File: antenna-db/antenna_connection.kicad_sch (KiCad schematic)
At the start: 2 parts

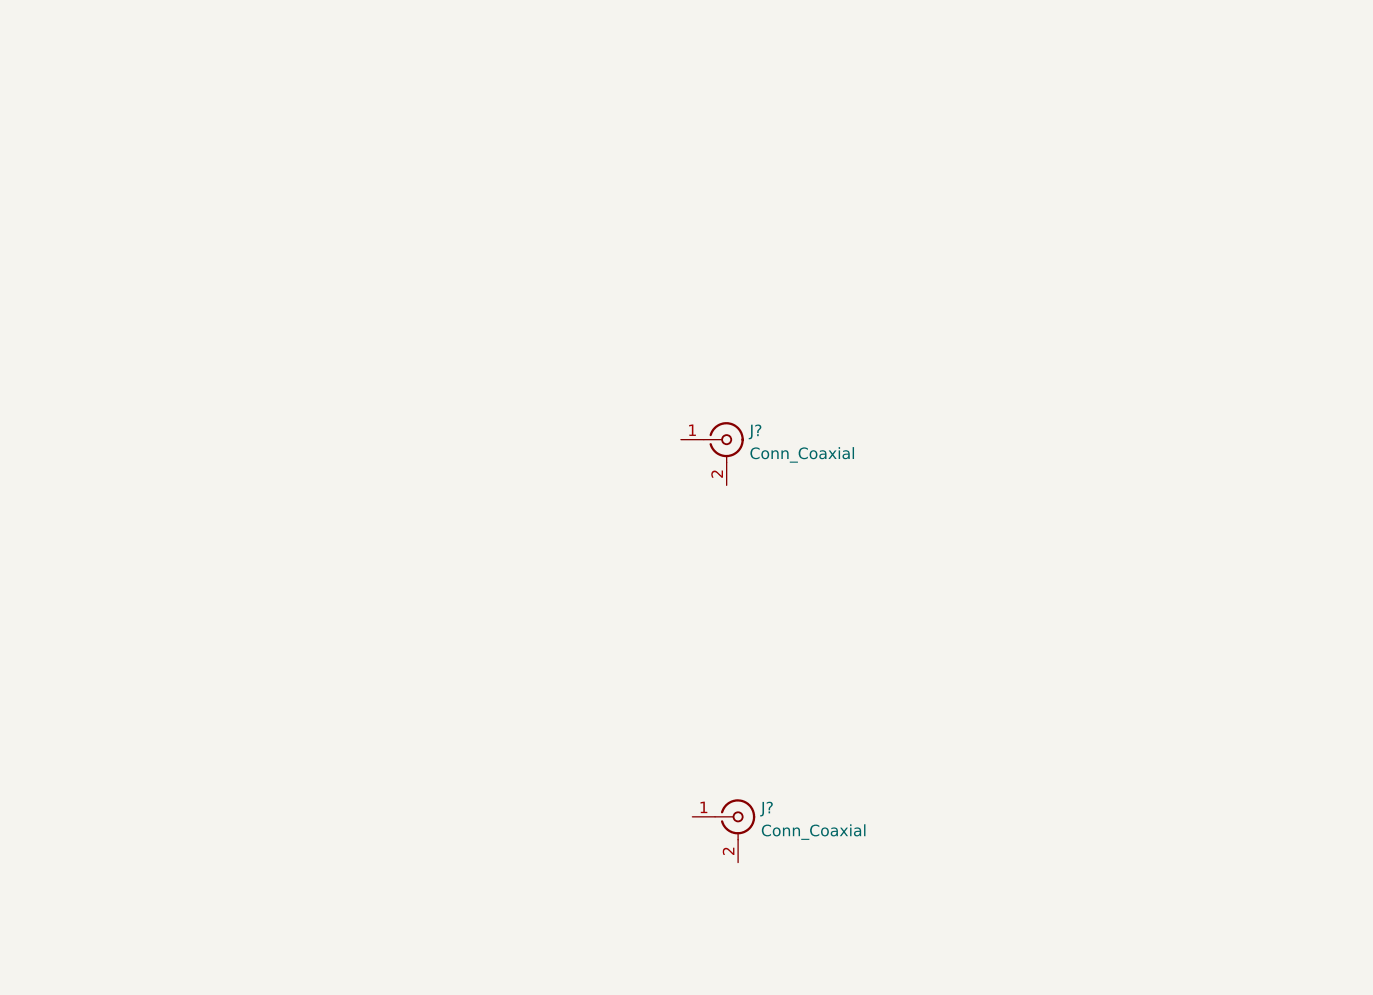
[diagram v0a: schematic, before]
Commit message: added baluns to antenna connection part
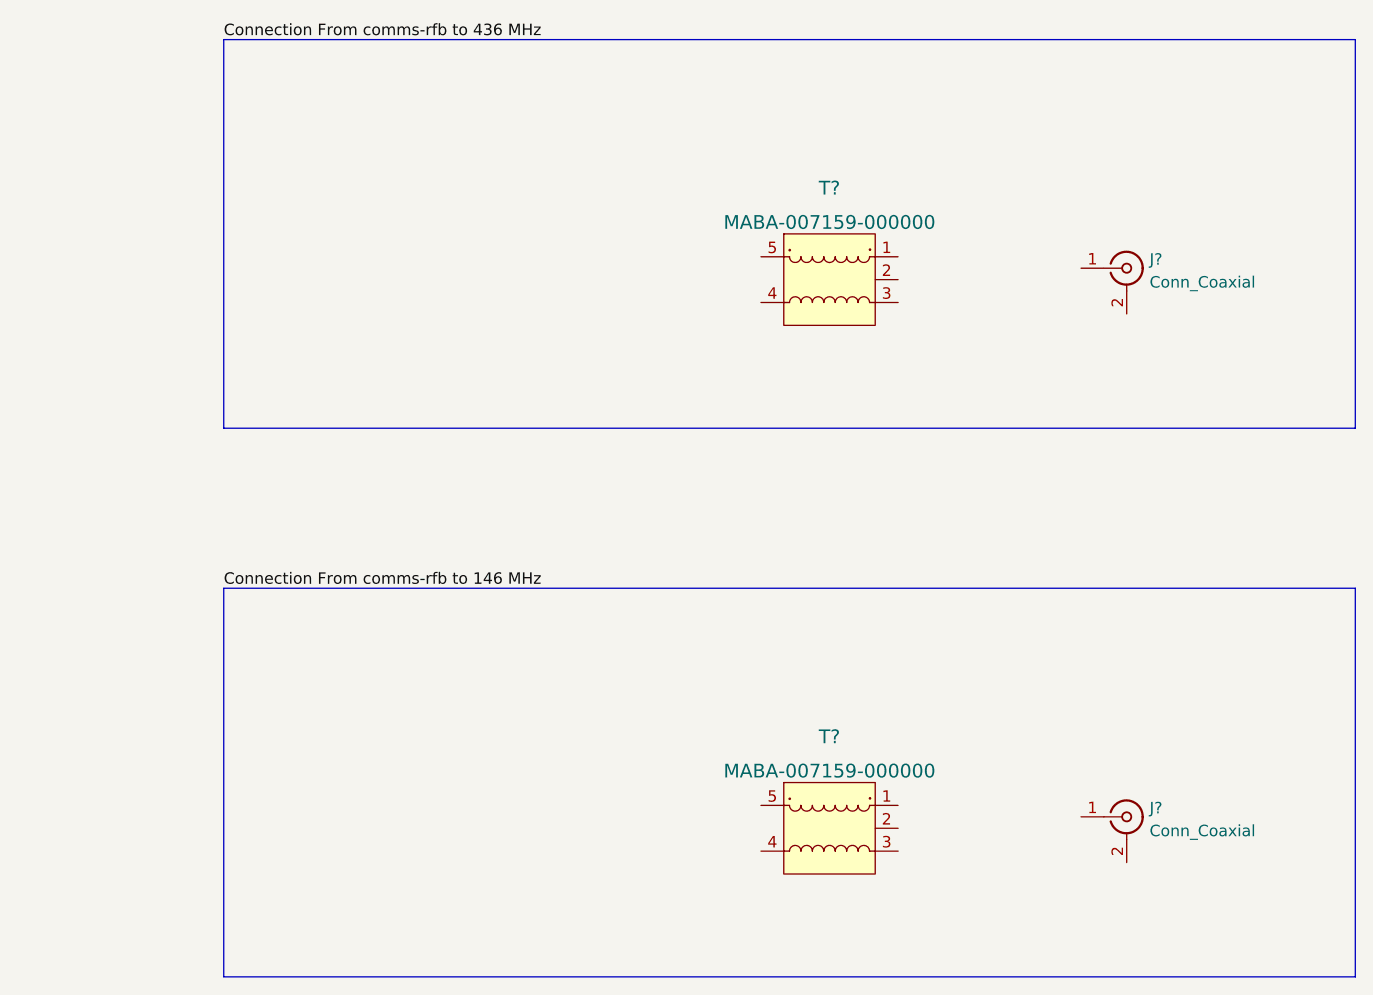
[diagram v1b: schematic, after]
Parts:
- removed J?: Conn_Coaxial, symbol Connector:Conn_Coaxial
- added J?: Conn_Coaxial, symbol Connector:Conn_Coaxial
- added T? (x2): MABA-007159-000000, digikey-footprints:SMD-5-6_3.83x2.79mm, symbol dk_Balun:MABA-007159-000000
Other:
- moved on the sheet: J?
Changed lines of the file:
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@@
 (kicad_sch (version 20211123) (generator eeschema)
   (paper "A4")
-  (symbol (lib_id "Connector:Conn_Coaxial") (at 160.02 80.01 0) (unit 1)
+  (polyline (pts (xy 104.14 96.52) (xy 229.87 96.52))
+    (stroke (width 0) (type default) (color 0 0 0 0))
+  )
+  (polyline (pts (xy 104.14 35.56) (xy 229.87 35.56))
+    (stroke (width 0) (type default) (color 0 0 0 0))
+  )
+  (polyline (pts (xy 229.87 78.74) (xy 104.14 78.74))
+    (stroke (width 0) (type default) (color 0 0 0 0))
+  )
+  (polyline (pts (xy 104.14 35.56) (xy 104.14 78.74))
+    (stroke (width 0) (type default) (color 0 0 0 0))
+  )
+  (polyline (pts (xy 104.14 96.52) (xy 104.14 139.7))
+    (stroke (width 0) (type default) (color 0 0 0 0))
+  )
+  (polyline (pts (xy 229.87 139.7) (xy 104.14 139.7))
+    (stroke (width 0) (type default) (color 0 0 0 0))
+  )
+  (polyline (pts (xy 229.87 96.52) (xy 229.87 139.7))
+    (stroke (width 0) (type default) (color 0 0 0 0))
+  )
+  (polyline (pts (xy 229.87 35.56) (xy 229.87 78.74))
+    (stroke (width 0) (type default) (color 0 0 0 0))
+  )
+  (label "Connection From comms-rfb to 146 MHz" (at 104.14 96.52 0)
+    (effects (font (size 1.27 1.27)) (justify left bottom))
+  )
+  (label "Connection From comms-rfb to 436 MHz" (at 104.14 35.56 0)
+    (effects (font (size 1.27 1.27)) (justify left bottom))
+  )
+  (symbol (lib_id "Connector:Conn_Coaxial") (at 204.47 60.96 0) (unit 1)
     (in_bom yes) (on_board yes) (fields_autoplaced)
-    (property "Reference" "J?" (id 0) (at 162.56 79.0331 0)
+    (property "Reference" "J?" (id 0) (at 207.01 59.9831 0)
       (effects (font (size 1.27 1.27)) (justify left))
     )
-    (property "Value" "Conn_Coaxial" (id 1) (at 162.56 81.5731 0)
+    (property "Value" "Conn_Coaxial" (id 1) (at 207.01 62.5231 0)
       (effects (font (size 1.27 1.27)) (justify left))
     )
-    (property "Footprint" "" (id 2) (at 160.02 80.01 0)
+    (property "Footprint" "" (id 2) (at 204.47 60.96 0)
       (effects (font (size 1.27 1.27)) hide)
     )
-    (property "Datasheet" " ~" (id 3) (at 160.02 80.01 0)
+    (property "Datasheet" " ~" (id 3) (at 204.47 60.96 0)
       (effects (font (size 1.27 1.27)) hide)
     )
@@
     (pin "2")
   )
-  (symbol (lib_id "Connector:Conn_Coaxial") (at 161.29 121.92 0) (unit 1)
+  (symbol (lib_id "dk_Balun:MABA-007159-000000") (at 171.45 62.23 0) (unit 1)
     (in_bom yes) (on_board yes) (fields_autoplaced)
-    (property "Reference" "J?" (id 0) (at 163.83 120.9431 0)
+    (property "Reference" "T?" (id 0) (at 171.45 52.07 0)
+      (effects (font (size 1.524 1.524)))
+    )
+    (property "Value" "MABA-007159-000000" (id 1) (at 171.45 55.88 0)
+      (effects (font (size 1.524 1.524)))
+    )
+    (property "Footprint" "digikey-footprints:SMD-5-6_3.83x2.79mm" (id 2) (at 176.53 57.15 0)
+      (effects (font (size 1.524 1.524)) (justify left) hide)
+    )
+    (property "Datasheet" "http://cdn.macom.com/datasheets/MABA-007159-000000.pdf" (id 3) (at 176.53 54.61 0)
+      (effects (font (size 1.524 1.524)) (justify left) hide)
+    )
+    (property "Digi-Key_PN" "1465-1302-1-ND" (id 4) (at 176.53 52.07 0)
+      (effects (font (size 1.524 1.524)) (justify left) hide)
+    )
+    (property "MPN" "MABA-007159-000000" (id 5) (at 176.53 49.53 0)
+      (effects (font (size 1.524 1.524)) (justify left) hide)
+    )
+    (property "Category" "RF/IF and RFID" (id 6) (at 176.53 46.99 0)
+      (effects (font (size 1.524 1.524)) (justify left) hide)
+    )
+    (property "Family" "Balun" (id 7) (at 176.53 44.45 0)
+      (effects (font (size 1.524 1.524)) (justify left) hide)
+    )
+    (property "DK_Datasheet_Link" "http://cdn.macom.com/datasheets/MABA-007159-000000.pdf" (id 8) (at 176.53 41.91 0)
+      (effects (font (size 1.524 1.524)) (justify left) hide)
+    )
+    (property "DK_Detail_Page" "/product-detail/en/m-a-com-technology-solutions/MABA-007159-000000/1465-1302-1-ND/4429999" (id 9) (at 176.53 39.37 0)
+      (effects (font (size 1.524 1.524)) (justify left) hide)
+    )
+    (property "Description" "BALUN 4.5MHZ-3GHZ 1:1 6SMD FLAT" (id 10) (at 176.53 36.83 0)
+      (effects (font (size 1.524 1.524)) (justify left) hide)
+    )
+    (property "Manufacturer" "M/A-Com Technology Solutions" (id 11) (at 176.53 34.29 0)
+      (effects (font (size 1.524 1.524)) (justify left) hide)
+    )
+    (property "Status" "Active" (id 12) (at 176.53 31.75 0)
+      (effects (font (size 1.524 1.524)) (justify left) hide)
+    )
+    (pin "2")
+    (pin "1")
+    (pin "3")
+    (pin "4")
+    (pin "5")
+  )
+  (symbol (lib_id "dk_Balun:MABA-007159-000000") (at 171.45 123.19 0) (unit 1)
+    (in_bom yes) (on_board yes) (fields_autoplaced)
+    (property "Reference" "T?" (id 0) (at 171.45 113.03 0)
+      (effects (font (size 1.524 1.524)))
+    )
+    (property "Value" "MABA-007159-000000" (id 1) (at 171.45 116.84 0)
+      (effects (font (size 1.524 1.524)))
+    )
+    (property "Footprint" "digikey-footprints:SMD-5-6_3.83x2.79mm" (id 2) (at 176.53 118.11 0)
+      (effects (font (size 1.524 1.524)) (justify left) hide)
+    )
+    (property "Datasheet" "http://cdn.macom.com/datasheets/MABA-007159-000000.pdf" (id 3) (at 176.53 115.57 0)
+      (effects (font (size 1.524 1.524)) (justify left) hide)
+    )
+    (property "Digi-Key_PN" "1465-1302-1-ND" (id 4) (at 176.53 113.03 0)
+      (effects (font (size 1.524 1.524)) (justify left) hide)
+    )
+    (property "MPN" "MABA-007159-000000" (id 5) (at 176.53 110.49 0)
+      (effects (font (size 1.524 1.524)) (justify left) hide)
+    )
+    (property "Category" "RF/IF and RFID" (id 6) (at 176.53 107.95 0)
+      (effects (font (size 1.524 1.524)) (justify left) hide)
+    )
+    (property "Family" "Balun" (id 7) (at 176.53 105.41 0)
+      (effects (font (size 1.524 1.524)) (justify left) hide)
+    )
+    (property "DK_Datasheet_Link" "http://cdn.macom.com/datasheets/MABA-007159-000000.pdf" (id 8) (at 176.53 102.87 0)
+      (effects (font (size 1.524 1.524)) (justify left) hide)
+    )
+    (property "DK_Detail_Page" "/product-detail/en/m-a-com-technology-solutions/MABA-007159-000000/1465-1302-1-ND/4429999" (id 9) (at 176.53 100.33 0)
+      (effects (font (size 1.524 1.524)) (justify left) hide)
+    )
+    (property "Description" "BALUN 4.5MHZ-3GHZ 1:1 6SMD FLAT" (id 10) (at 176.53 97.79 0)
+      (effects (font (size 1.524 1.524)) (justify left) hide)
+    )
+    (property "Manufacturer" "M/A-Com Technology Solutions" (id 11) (at 176.53 95.25 0)
+      (effects (font (size 1.524 1.524)) (justify left) hide)
+    )
+    (property "Status" "Active" (id 12) (at 176.53 92.71 0)
+      (effects (font (size 1.524 1.524)) (justify left) hide)
+    )
+    (pin "2")
+    (pin "1")
+    (pin "3")
+    (pin "4")
+    (pin "5")
+  )
+  (symbol (lib_id "Connector:Conn_Coaxial") (at 204.47 121.92 0) (unit 1)
+    (in_bom yes) (on_board yes) (fields_autoplaced)
+    (property "Reference" "J?" (id 0) (at 207.01 120.9431 0)
       (effects (font (size 1.27 1.27)) (justify left))
     )
-    (property "Value" "Conn_Coaxial" (id 1) (at 163.83 123.4831 0)
+    (property "Value" "Conn_Coaxial" (id 1) (at 207.01 123.4831 0)
       (effects (font (size 1.27 1.27)) (justify left))
     )
-    (property "Footprint" "" (id 2) (at 161.29 121.92 0)
+    (property "Footprint" "" (id 2) (at 204.47 121.92 0)
       (effects (font (size 1.27 1.27)) hide)
     )
-    (property "Datasheet" " ~" (id 3) (at 161.29 121.92 0)
+    (property "Datasheet" " ~" (id 3) (at 204.47 121.92 0)
       (effects (font (size 1.27 1.27)) hide)
     )

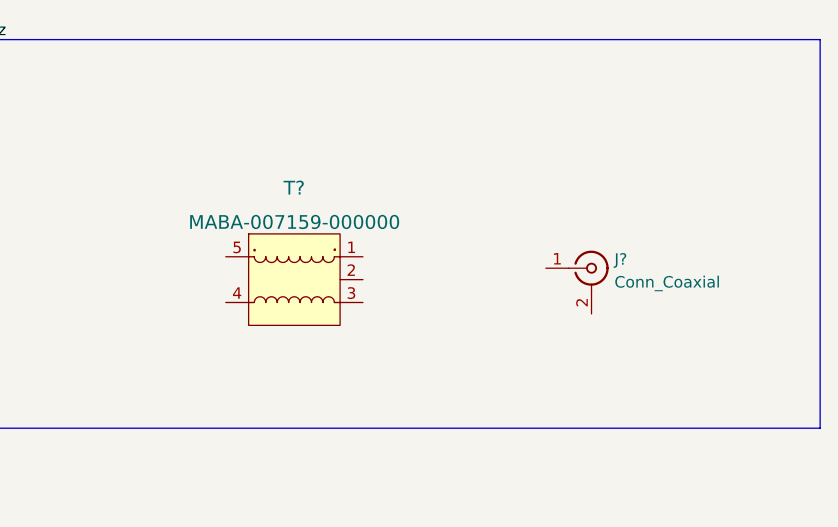
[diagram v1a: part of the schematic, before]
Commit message: added regulator symbol ~ not circuit yet
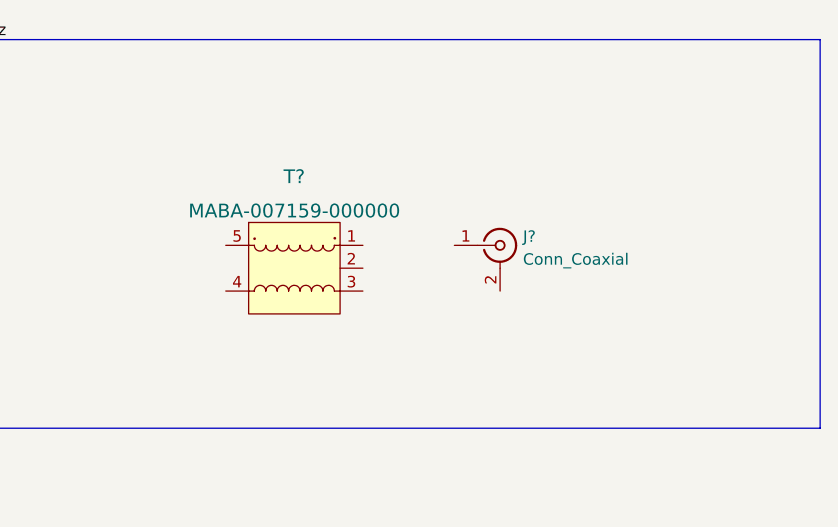
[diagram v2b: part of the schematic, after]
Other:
- moved on the sheet: J?, T?
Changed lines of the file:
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@@
     (effects (font (size 1.27 1.27)) (justify left bottom))
   )
-  (symbol (lib_id "Connector:Conn_Coaxial") (at 204.47 60.96 0) (unit 1)
+  (symbol (lib_id "Connector:Conn_Coaxial") (at 194.31 58.42 0) (unit 1)
     (in_bom yes) (on_board yes) (fields_autoplaced)
-    (property "Reference" "J?" (id 0) (at 207.01 59.9831 0)
+    (property "Reference" "J?" (id 0) (at 196.85 57.4431 0)
       (effects (font (size 1.27 1.27)) (justify left))
     )
-    (property "Value" "Conn_Coaxial" (id 1) (at 207.01 62.5231 0)
+    (property "Value" "Conn_Coaxial" (id 1) (at 196.85 59.9831 0)
       (effects (font (size 1.27 1.27)) (justify left))
     )
-    (property "Footprint" "" (id 2) (at 204.47 60.96 0)
+    (property "Footprint" "" (id 2) (at 194.31 58.42 0)
       (effects (font (size 1.27 1.27)) hide)
     )
-    (property "Datasheet" " ~" (id 3) (at 204.47 60.96 0)
+    (property "Datasheet" " ~" (id 3) (at 194.31 58.42 0)
       (effects (font (size 1.27 1.27)) hide)
     )
@@
     (pin "2")
   )
-  (symbol (lib_id "dk_Balun:MABA-007159-000000") (at 171.45 62.23 0) (unit 1)
+  (symbol (lib_id "dk_Balun:MABA-007159-000000") (at 171.45 60.96 0) (unit 1)
     (in_bom yes) (on_board yes) (fields_autoplaced)
-    (property "Reference" "T?" (id 0) (at 171.45 52.07 0)
+    (property "Reference" "T?" (id 0) (at 171.45 50.8 0)
       (effects (font (size 1.524 1.524)))
     )
-    (property "Value" "MABA-007159-000000" (id 1) (at 171.45 55.88 0)
+    (property "Value" "MABA-007159-000000" (id 1) (at 171.45 54.61 0)
       (effects (font (size 1.524 1.524)))
     )
-    (property "Footprint" "digikey-footprints:SMD-5-6_3.83x2.79mm" (id 2) (at 176.53 57.15 0)
+    (property "Footprint" "digikey-footprints:SMD-5-6_3.83x2.79mm" (id 2) (at 176.53 55.88 0)
       (effects (font (size 1.524 1.524)) (justify left) hide)
     )
-    (property "Datasheet" "http://cdn.macom.com/datasheets/MABA-007159-000000.pdf" (id 3) (at 176.53 54.61 0)
+    (property "Datasheet" "http://cdn.macom.com/datasheets/MABA-007159-000000.pdf" (id 3) (at 176.53 53.34 0)
       (effects (font (size 1.524 1.524)) (justify left) hide)
     )
-    (property "Digi-Key_PN" "1465-1302-1-ND" (id 4) (at 176.53 52.07 0)
+    (property "Digi-Key_PN" "1465-1302-1-ND" (id 4) (at 176.53 50.8 0)
       (effects (font (size 1.524 1.524)) (justify left) hide)
     )
-    (property "MPN" "MABA-007159-000000" (id 5) (at 176.53 49.53 0)
+    (property "MPN" "MABA-007159-000000" (id 5) (at 176.53 48.26 0)
       (effects (font (size 1.524 1.524)) (justify left) hide)
     )
-    (property "Category" "RF/IF and RFID" (id 6) (at 176.53 46.99 0)
+    (property "Category" "RF/IF and RFID" (id 6) (at 176.53 45.72 0)
       (effects (font (size 1.524 1.524)) (justify left) hide)
     )
-    (property "Family" "Balun" (id 7) (at 176.53 44.45 0)
+    (property "Family" "Balun" (id 7) (at 176.53 43.18 0)
       (effects (font (size 1.524 1.524)) (justify left) hide)
     )
-    (property "DK_Datasheet_Link" "http://cdn.macom.com/datasheets/MABA-007159-000000.pdf" (id 8) (at 176.53 41.91 0)
+    (property "DK_Datasheet_Link" "http://cdn.macom.com/datasheets/MABA-007159-000000.pdf" (id 8) (at 176.53 40.64 0)
       (effects (font (size 1.524 1.524)) (justify left) hide)
     )
-    (property "DK_Detail_Page" "/product-detail/en/m-a-com-technology-solutions/MABA-007159-000000/1465-1302-1-ND/4429999" (id 9) (at 176.53 39.37 0)
+    (property "DK_Detail_Page" "/product-detail/en/m-a-com-technology-solutions/MABA-007159-000000/1465-1302-1-ND/4429999" (id 9) (at 176.53 38.1 0)
       (effects (font (size 1.524 1.524)) (justify left) hide)
     )
-    (property "Description" "BALUN 4.5MHZ-3GHZ 1:1 6SMD FLAT" (id 10) (at 176.53 36.83 0)
+    (property "Description" "BALUN 4.5MHZ-3GHZ 1:1 6SMD FLAT" (id 10) (at 176.53 35.56 0)
       (effects (font (size 1.524 1.524)) (justify left) hide)
     )
-    (property "Manufacturer" "M/A-Com Technology Solutions" (id 11) (at 176.53 34.29 0)
+    (property "Manufacturer" "M/A-Com Technology Solutions" (id 11) (at 176.53 33.02 0)
       (effects (font (size 1.524 1.524)) (justify left) hide)
     )
-    (property "Status" "Active" (id 12) (at 176.53 31.75 0)
+    (property "Status" "Active" (id 12) (at 176.53 30.48 0)
       (effects (font (size 1.524 1.524)) (justify left) hide)
     )
